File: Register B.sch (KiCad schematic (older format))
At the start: 2 parts

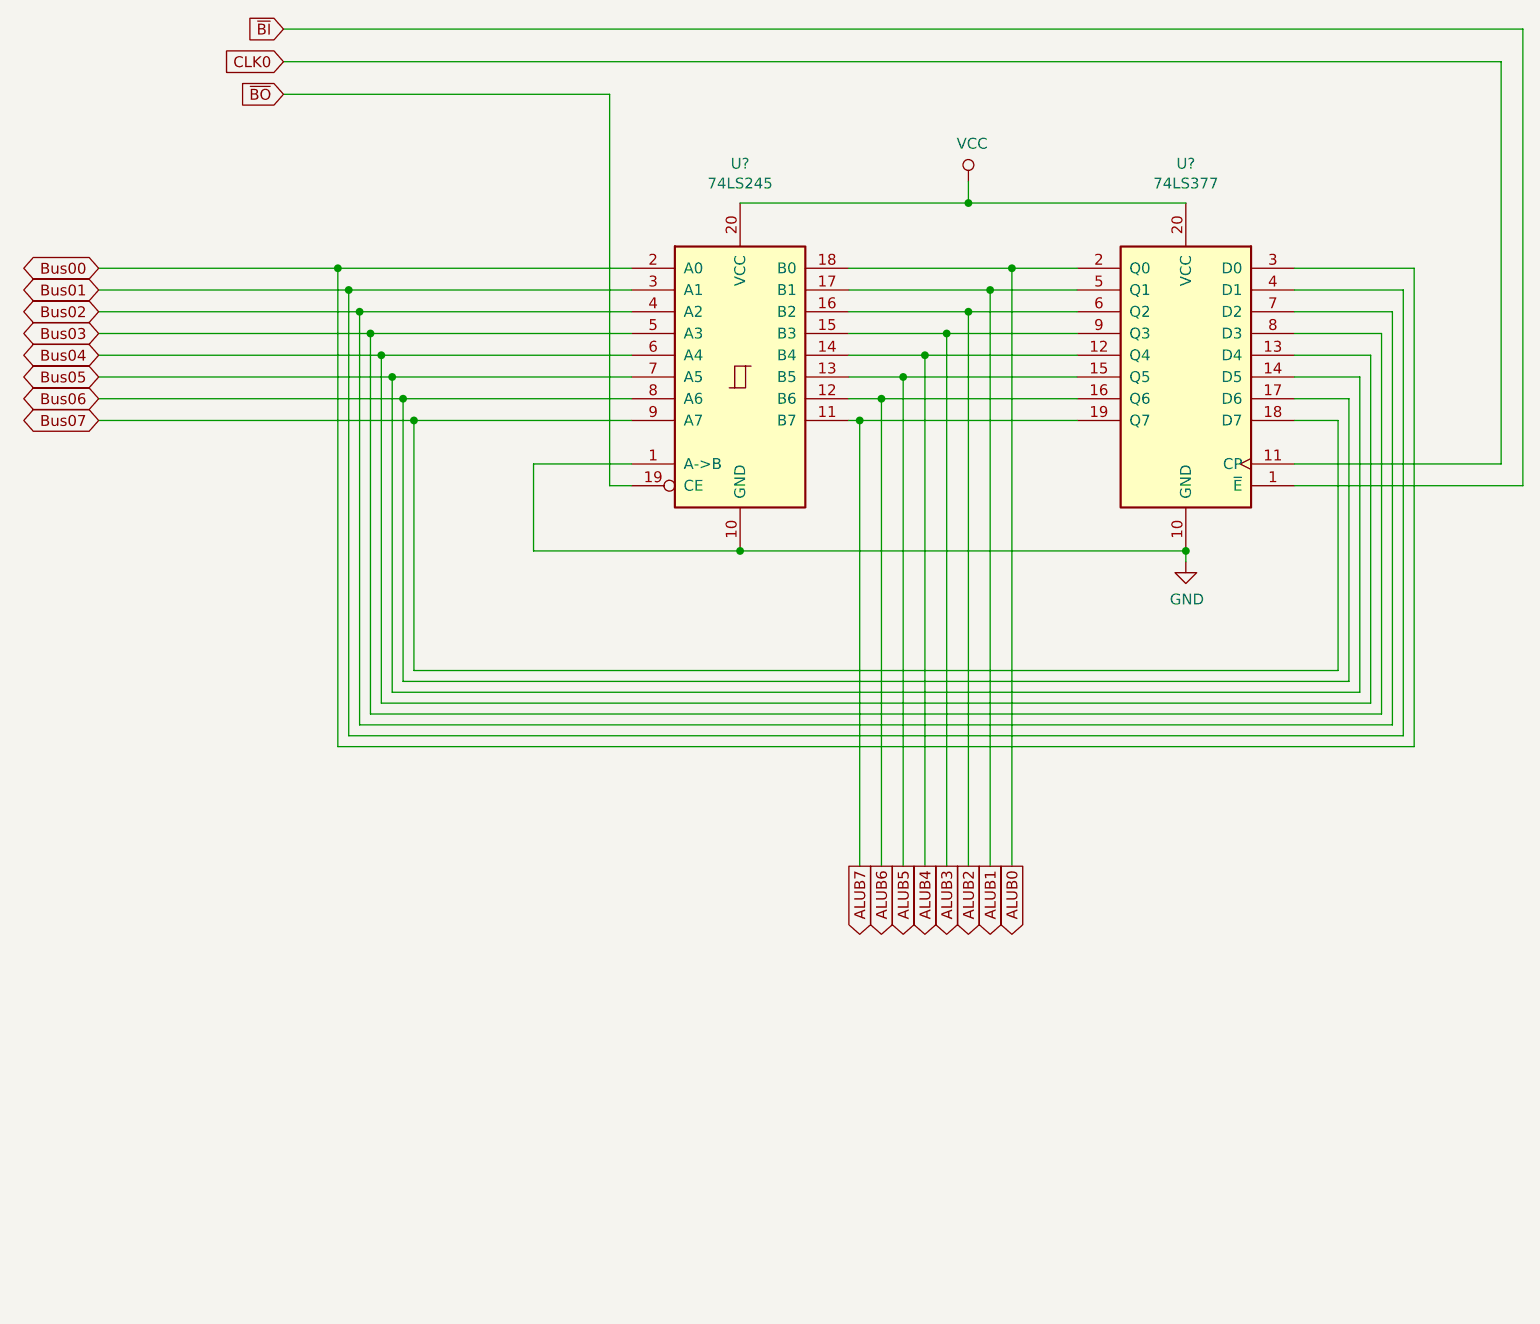
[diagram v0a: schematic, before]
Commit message: Add LEDs to registers A and B.
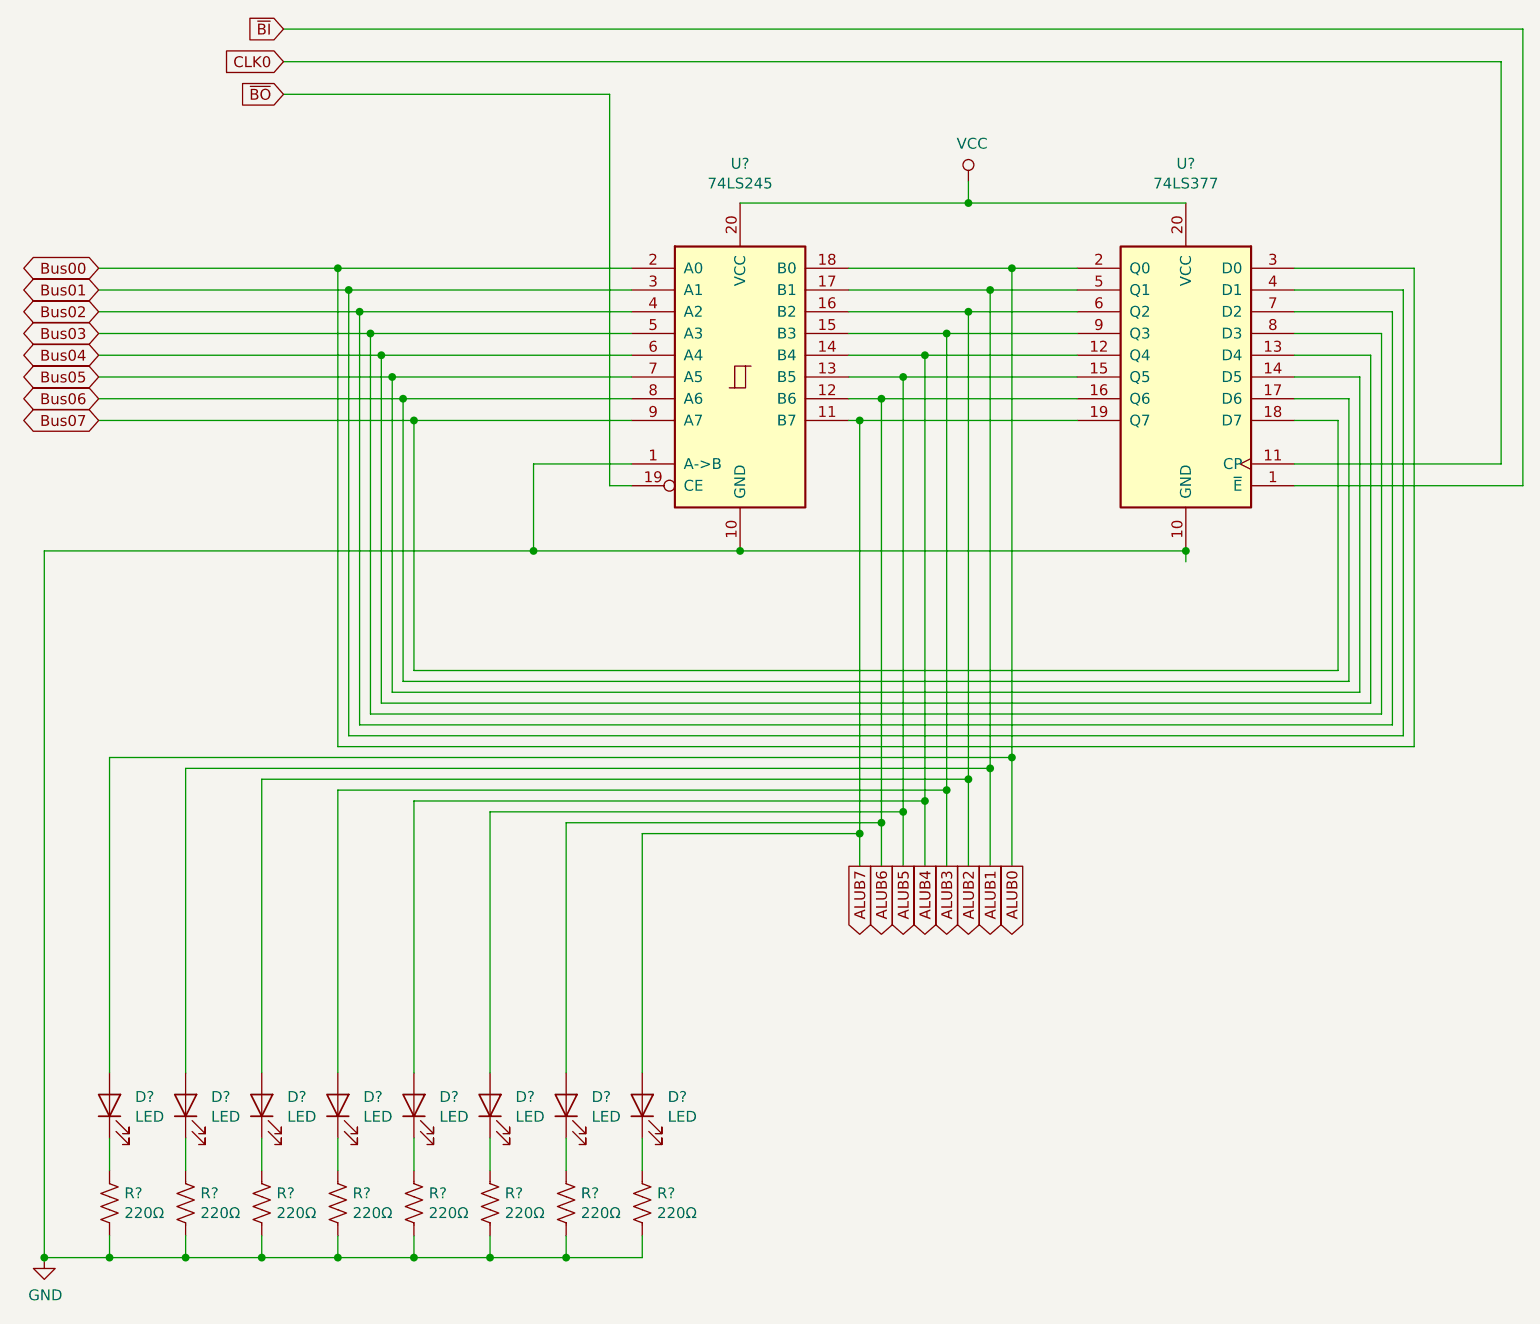
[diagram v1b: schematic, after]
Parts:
- added D? (x8): LED, symbol Device:LED
- added R? (x8): 220Ω, symbol Device:R_US
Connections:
- net ALUB0: now also D?.2 (A)
- net ALUB1: now also D?.2 (A)
- net ALUB2: now also D?.2 (A)
- net ALUB3: now also D?.2 (A)
- net ALUB4: now also D?.2 (A)
- net ALUB5: now also D?.2 (A)
- net ALUB6: now also D?.2 (A)
- net ALUB7: now also D?.2 (A)
- net GND: now also R?.2, R?.2, R?.2, R?.2, R?.2, R?.2, R?.2, R?.2
- new net: D?.1 (K), R?.1 (x8)

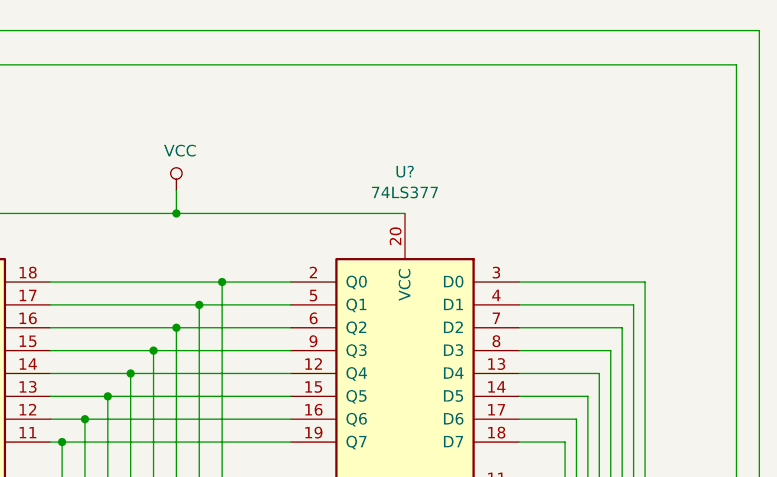
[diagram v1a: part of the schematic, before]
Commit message: Some of these chips actually need to be 74F not 74LS.
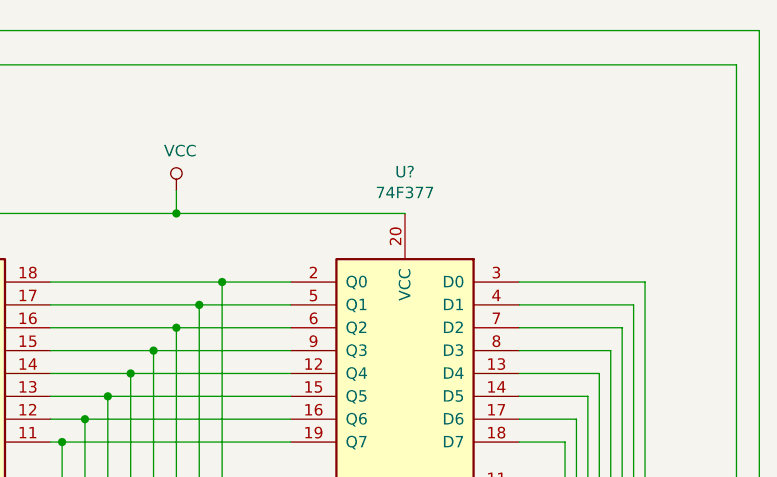
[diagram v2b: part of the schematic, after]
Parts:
- U?: value 74LS377 -> 74F377
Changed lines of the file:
@@
 AR Path="/5D2C0D13/5D29B693" Ref="U?"  Part="1"
 F 0 "U?" H 7350 4281 50  0000 C CNN
-F 1 "74LS377" H 7350 4190 50  0000 C CNN
+F 1 "74F377" H 7350 4190 50  0000 C CNN
 F 2 "" H 7350 3300 50  0001 C CNN
 F 3 "http://www.ti.com/lit/gpn/sn74LS377" H 7350 3300 50  0001 C CNN
